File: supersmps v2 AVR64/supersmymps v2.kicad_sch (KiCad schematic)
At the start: 136 parts, among them J1 c21 socket, J2 programmer, J3 Front_Panel, J4 Conn_01x03_Socket, J5 Wire (it's copper), Q1 IRFP360, Q2 IRFP360, Q3 IRFP360, Q4 IRFP360, Q5 IRFP360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

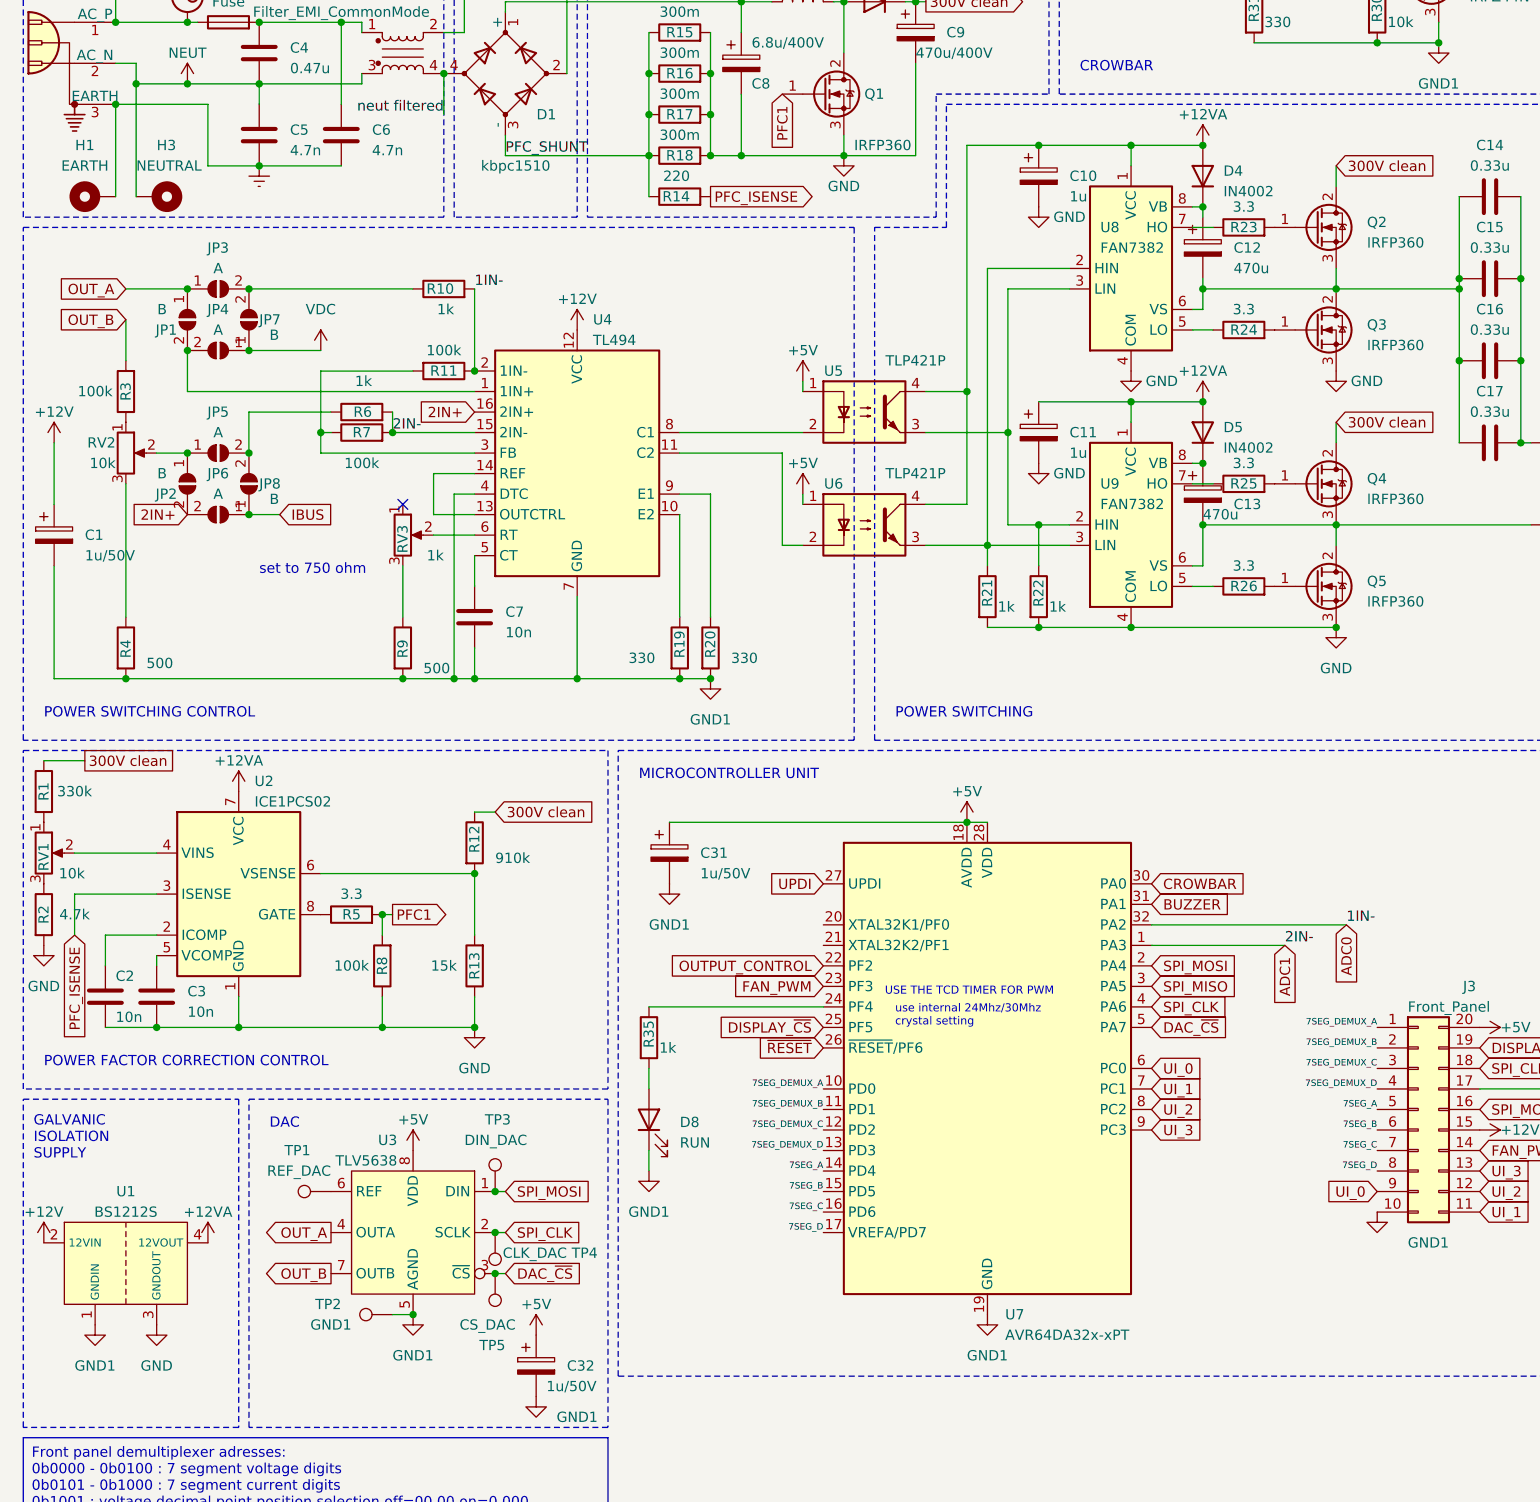
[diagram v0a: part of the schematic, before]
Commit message: One of the last versions before prototype is done.
I have finally gotten rid of the solder jumpers because i'm now sure how the tl494 circuit works
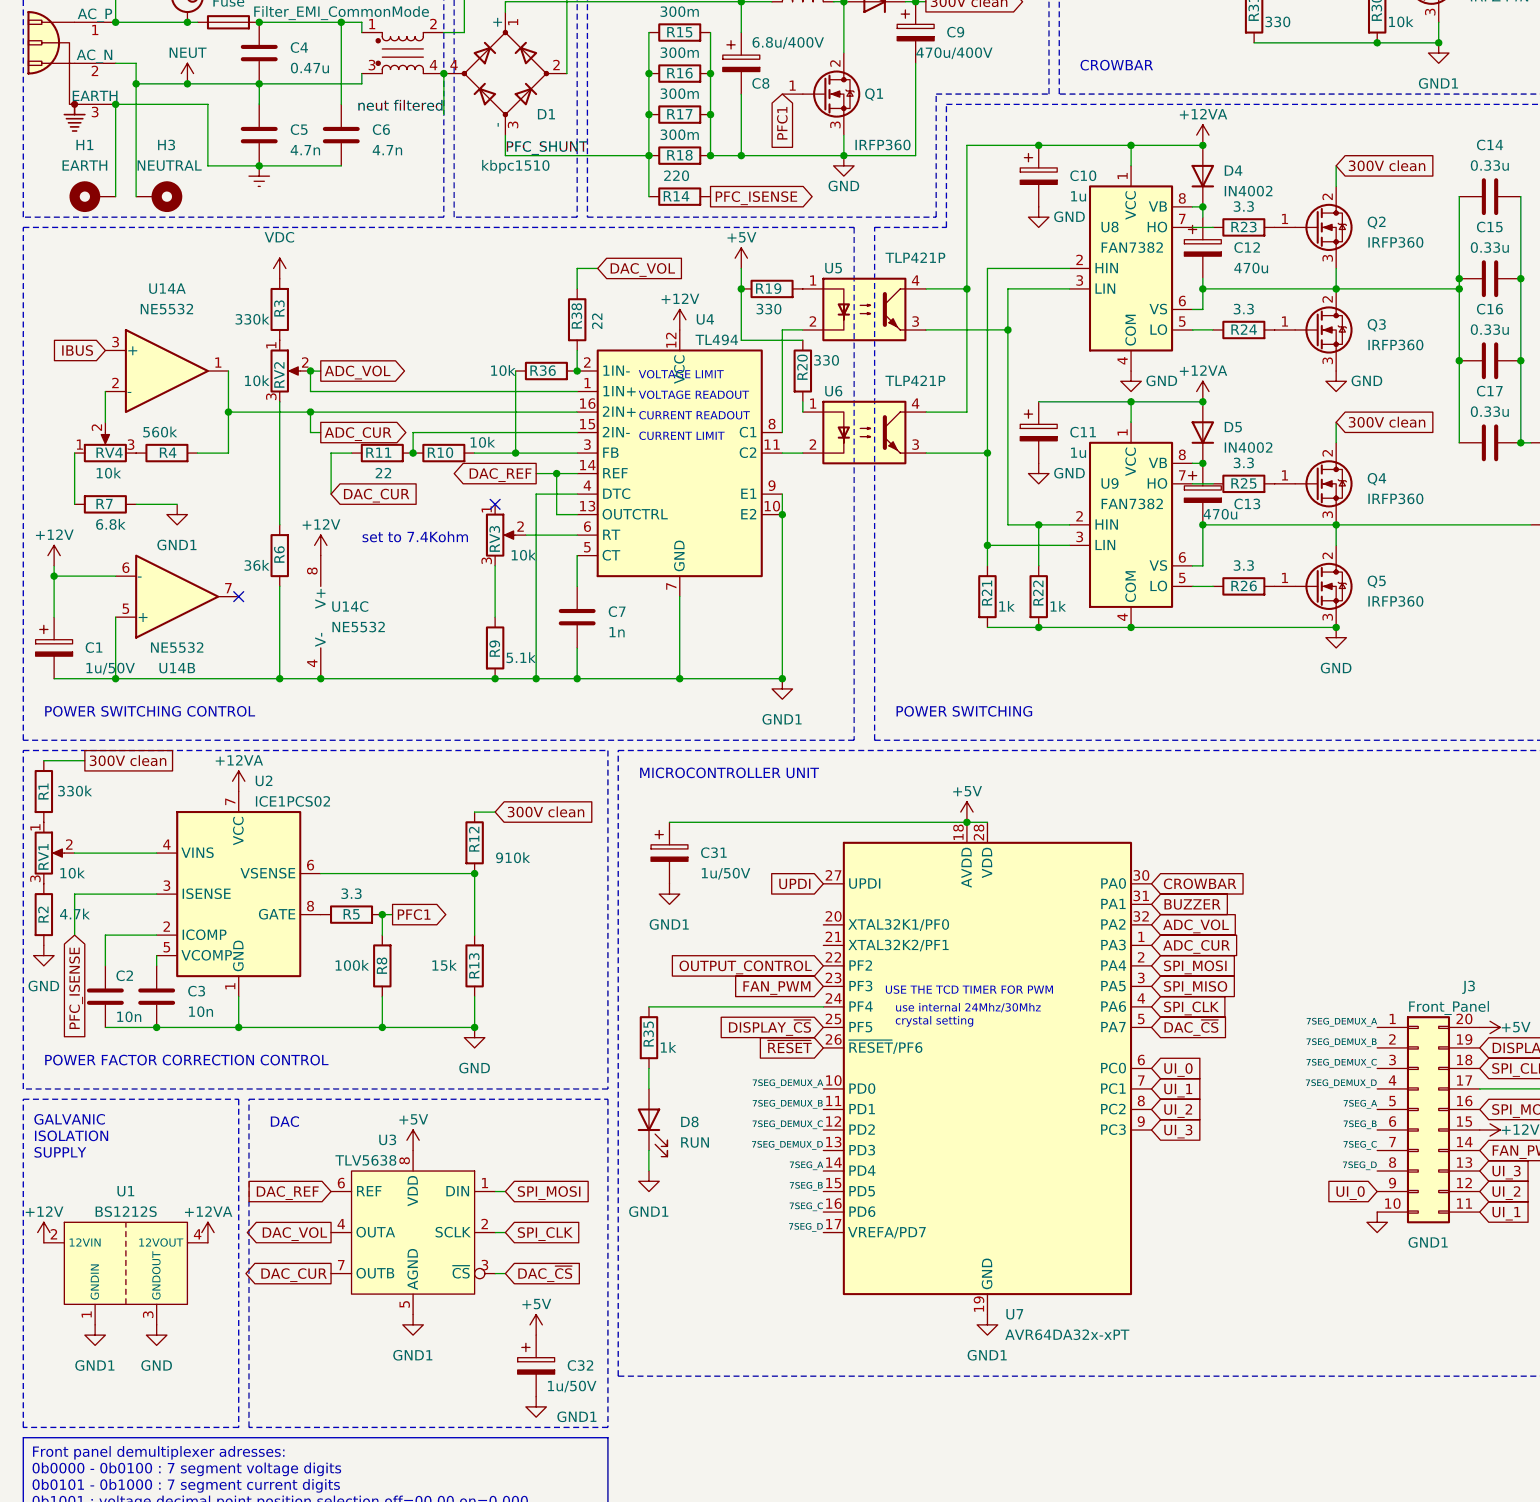
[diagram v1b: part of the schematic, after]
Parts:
- removed JP1, JP2, JP7, JP8: B, Jumper:SolderJumper-2_P1.3mm_Open_RoundedPad1.0x1.5mm, symbol Jumper:SolderJumper_2_Open
- removed JP3, JP4, JP5, JP6: A, Jumper:SolderJumper-2_P1.3mm_Open_RoundedPad1.0x1.5mm, symbol Jumper:SolderJumper_2_Open
- removed TP1: REF_DAC, TestPoint:TestPoint_Pad_D2.0mm, symbol Connector:TestPoint
- removed TP2: GND1, TestPoint:TestPoint_Pad_D2.0mm, symbol Connector:TestPoint
- removed TP3: DIN_DAC, TestPoint:TestPoint_Pad_D2.0mm, symbol Connector:TestPoint
- removed TP4: CLK_DAC, TestPoint:TestPoint_Pad_D2.0mm, symbol Connector:TestPoint
- removed TP5: CS_DAC, TestPoint:TestPoint_Pad_D2.0mm, symbol Connector:TestPoint
- added R36: 10k, Resistor_THT:R_Axial_DIN0204_L3.6mm_D1.6mm_P5.08mm_Horizontal, symbol Device:R
- added R38: 22, Resistor_THT:R_Axial_DIN0207_L6.3mm_D2.5mm_P7.62mm_Horizontal, symbol Device:R
- added RV4: 10k, Potentiometer_THT:Potentiometer_Bourns_3296W_Vertical, symbol Device:R_Potentiometer
- added U14: NE5532, Package_DIP:DIP-8_W7.62mm, symbol Amplifier_Operational:NE5532
- C7: value 10n -> 1n
- R10, RV3: value 1k -> 10k
- R11: value 100k -> 22; footprint Resistor_THT:R_Axial_DIN0207_L6.3mm_D2.5mm_P10.16mm_Horizontal -> Resistor_THT:R_Axial_DIN0207_L6.3mm_D2.5mm_P7.62mm_Horizontal
- R19, R20: footprint Resistor_THT:R_Axial_DIN0207_L6.3mm_D2.5mm_P10.16mm_Horizontal -> Resistor_THT:R_Axial_DIN0207_L6.3mm_D2.5mm_P7.62mm_Horizontal
- R3: value 100k -> 330k; footprint Resistor_THT:R_Axial_DIN0207_L6.3mm_D2.5mm_P10.16mm_Horizontal -> Resistor_THT:R_Axial_DIN0207_L6.3mm_D2.5mm_P7.62mm_Horizontal
- R4: value 500 -> 560k; footprint Resistor_THT:R_Axial_DIN0207_L6.3mm_D2.5mm_P10.16mm_Horizontal -> Resistor_THT:R_Axial_DIN0207_L6.3mm_D2.5mm_P7.62mm_Horizontal
- R6: value 1k -> 36k; footprint Resistor_THT:R_Axial_DIN0204_L3.6mm_D1.6mm_P5.08mm_Horizontal -> Resistor_THT:R_Axial_DIN0207_L6.3mm_D2.5mm_P7.62mm_Horizontal
- R7: value 100k -> 6.8k; footprint Resistor_THT:R_Axial_DIN0207_L6.3mm_D2.5mm_P10.16mm_Horizontal -> Resistor_THT:R_Axial_DIN0207_L6.3mm_D2.5mm_P7.62mm_Horizontal
- R9: value 500 -> 5.1k; footprint Resistor_THT:R_Axial_DIN0207_L6.3mm_D2.5mm_P10.16mm_Horizontal -> Resistor_THT:R_Axial_DIN0207_L6.3mm_D2.5mm_P7.62mm_Horizontal
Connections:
- net +12V: now also U14.6 (-), U14.8 (V+)
- net +5V: now also R19.1, R20.1; no longer U5.1, U6.1
- net GND1: now also R6.1, R7.1, U4.10 (E2), U4.9 (E1), U14.4 (V-), U14.5 (+); no longer R19.2, R20.2, R4.2
- net IBUS: now also U14.3 (+)
- net VDC: now also R3.2
- net ADC_VOL: now reaches U4.1 (1IN+)
- net ADC_VOL: now also RV2.2, U7.32 (PA2)
- net DAC_REF: now reaches U3.6 (REF)
- net DAC_REF: now also U4.13 (OUTCTRL), U4.14 (REF)
- net at R4.1: now also RV4.3; no longer RV2.3
- net at R10.1: now also R11.2, U4.15 (2IN-)
- net 2IN+ renamed ADC_CUR
- net ADC_CUR: now also R4.2, U7.1 (PA3), U14.1
- removed net ADC0: R10.2, R11.1, U4.2 (1IN-), U7.32 (PA2)
- removed net ADC1: R6.2, R7.2, U4.15 (2IN-), U7.1 (PA3)
- net OUT_A renamed DAC_VOL
- net DAC_VOL: now also R38.1
- net OUT_B renamed DAC_CUR
- net DAC_CUR: now also R11.1; no longer R3.2
- new net: R7.2, RV4.1
- new net: R20.2, U6.1
- new net: R36.2, R38.2, U4.2 (1IN-)
- new net: RV4.2, U14.2 (-)
- new net: R6.2, RV2.3
- new net: R19.2, U5.1
- new net: R10.2, R36.1, U4.3 (FB)
- no-connect marks 2 -> 3
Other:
- note added: "CURRENT LIMIT"
- note added: "CURRENT READOUT"
- note added: "VOLTAGE LIMIT"
- note added: "VOLTAGE READOUT"
- note added: "set to 7.4Kohm"
- note removed: "set to 750 ohm"
- moved on the sheet: C1, C7, R19, R20, R9, RV2, RV3, U4, U5, U6
